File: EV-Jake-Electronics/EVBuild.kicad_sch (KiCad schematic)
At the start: 15 parts, among them J1 Spark Max PWM Pins, J2 Spark Max PWM Pins, U1 ESP32-S3-WROOM-2

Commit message: laser
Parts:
- removed C1: .1, symbol Device:C
- removed FlyDragon1: ~, symbol FlyDragon:FlyDragon
- removed J1: Spark Max PWM Pins, Connector_JST:JST_PH_S4B-PH-K_1x04_P2.00mm_Horizontal, symbol Connector:Conn_01x04_Socket
- removed LSF1: ~, symbol LSF0102:LSF0102
- removed R1: 220, symbol Device:R
- removed U1: ESP32-S3-WROOM-2, RF_Module:ESP32-S3-WROOM-2, symbol RF_Module:ESP32-S3-WROOM-2
- removed U2: ~, symbol LSF0104:LSF0104
- added C5: .1u, symbol Device:C
- added LSF2: ~, symbol LSF0104:LSF0104
- added R2: 220, symbol Device:R
- added R6, R7, R8, R9: 1k, Resistor_SMD:R_0201_0603Metric, symbol Device:R
- added SW1, SW2, SW3, SW4: SW_Push, Button_Switch_Keyboard:SW_Cherry_MX_1.00u_PCB, symbol Switch:SW_Push
- added U1: ESP32-WROOM-32, RF_Module:ESP32-WROOM-32, symbol RF_Module:ESP32-WROOM-32
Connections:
- net +5V: now also LSF2.7 (Vref_B), R2.1
- net 3V3: now also NCP1. (Vo), U1.2 (VDD)
- net CS: now also U1.24 (IO2)
- net FD 5V PWM: now also LSF2.7 (Vref_B)
- net GND: now also NCP1. (Vo), U3.1 (GND), C5.2, LSF2.6 (GND), R6.1, R7.1, R8.1, R9.1, U1.1 (GND), U1.15 (GND), U1.38 (GND), U1.39 (GND)
- net INT1: now also U1.14 (IO12)
- net INT2: now also U1.16 (IO13)
- net MISO: now also U1.29 (IO5)
- net MOSI: now also U1.26 (IO4)
- net SCK: now also U1.34 (RXD0/IO3)
- net SM 5V PWM 1: now also LSF2.8 (B2)
- net SM 5V PWM 2: now also LSF2.9 (B3)
- net VCC: now also NCP1. (Vo), U3.2 (VCC), R6.2, SW1.1, SW2.1, SW3.1, SW4.1, SW4.2, U1.12 (IO27)
- net OLED_SDA: now reaches U3.3 (SDA)
- net OLED_SDA: now also U1.33 (IO21)
- net OLED_SCL: now reaches U3.4 (SCL)
- net OLED_SCL: now also U1.36 (IO22)
- new net: C5.1, R2.2
- new net +3V3: LSF2.1 (Vref_A)
- new net BTN0: R9.2, SW1.2, U1.37 (IO23)
- new net BTN1: R8.2, SW2.2, U1.10 (IO25)
- new net BTN2: R7.2, SW3.2, U1.11 (IO26)
- new net FD 3V3 PWM: LSF2.2 (A1), U1.27 (IO16)
- new net SM 3V3 PWM 1: LSF2.3 (A2), U1.23 (IO15)
- new net SM 3V3 PWM 2: LSF2.4 (A3), U1.13 (IO14)
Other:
- note added: "Accelerometer"
- note added: "Battery"
- note added: "User Interface"
- moved on the sheet: FlyDragon2, NCP1

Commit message: .
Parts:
- added Laser1: ~, symbol laser:Laser
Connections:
- no-connect marks 4 -> 6
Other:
- note added: "Laser"
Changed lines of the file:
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@@
   (no_connect (at 254 114.3))
   (no_connect (at 254 119.38))
+  (no_connect (at 207.01 36.83))
+  (no_connect (at 226.06 36.83))
   (wire (pts (xy 209.55 115.57) (xy 209.55 104.14))
     (stroke (width 0) (type default))
@@
     (stroke (width 0) (type default))
   )
+  (rectangle (start 35.56 91.44) (end 54.61 119.38)
+    (stroke (width 0) (type default))
+    (fill (type none))
+  )
   (rectangle (start 186.69 13.97) (end 283.21 66.04)
     (stroke (width 0) (type default))
@@
   )
   (text "Battery" (at 15.24 74.93 0)
+    (effects (font (size 1.27 1.27)) (justify left bottom))
+  )
+  (text "Laser\n" (at 36.83 116.84 0)
     (effects (font (size 1.27 1.27)) (justify left bottom))
   )
@@
     )
   )
+  (symbol (lib_id "laser:Laser") (at 44.45 109.22 0) (unit 1)
+    (in_bom yes) (on_board yes) (dnp no) (fields_autoplaced)
+    (property "Reference" "Laser1" (at 46.99 102.87 0)
+      (effects (font (size 1.27 1.27)) (justify left))
+    )
+    (property "Value" "~" (at 34.29 113.03 0)
+      (effects (font (size 1.27 1.27)))
+    )
+    (property "Footprint" "" (at 34.29 113.03 0)
+      (effects (font (size 1.27 1.27)) hide)
+    )
+    (property "Datasheet" "" (at 34.29 113.03 0)
+      (effects (font (size 1.27 1.27)) hide)
+    )
+    (pin "")
+    (pin "")
+    (instances
+      (project "EVBuild"
+        (path "/2997cb29-a416-41db-a9e8-1a576f951325"
+          (reference "Laser1") (unit 1)
+        )
+      )
+    )
+  )
   (symbol (lib_id "Switch:SW_Push") (at 45.72 163.83 0) (unit 1)
     (in_bom yes) (on_board yes) (dnp no)
@@
         )
       )
+    )
+  )
+  (symbol (lib_id "power:GND") (at 245.11 214.63 0) (unit 1)
+    (in_bom yes) (on_board yes) (dnp no) (fields_autoplaced)
+    (property "Reference" "#PWR06" (at 245.11 220.98 0)
+      (effects (font (size 1.27 1.27)) hide)
+    )
+    (property "Value" "GND" (at 245.11 219.71 0)
+      (effects (font (size 1.27 1.27)))
+    )
+    (property "Footprint" "" (at 245.11 214.63 0)
+      (effects (font (size 1.27 1.27)) hide)
+    )
+    (property "Datasheet" "" (at 245.11 214.63 0)
+      (effects (font (size 1.27 1.27)) hide)
+    )
+    (pin "1")
+    (instances
+      (project "EVBuild"
+        (path "/2997cb29-a416-41db-a9e8-1a576f951325"
+          (reference "#PWR06") (unit 1)
+        )
+      )

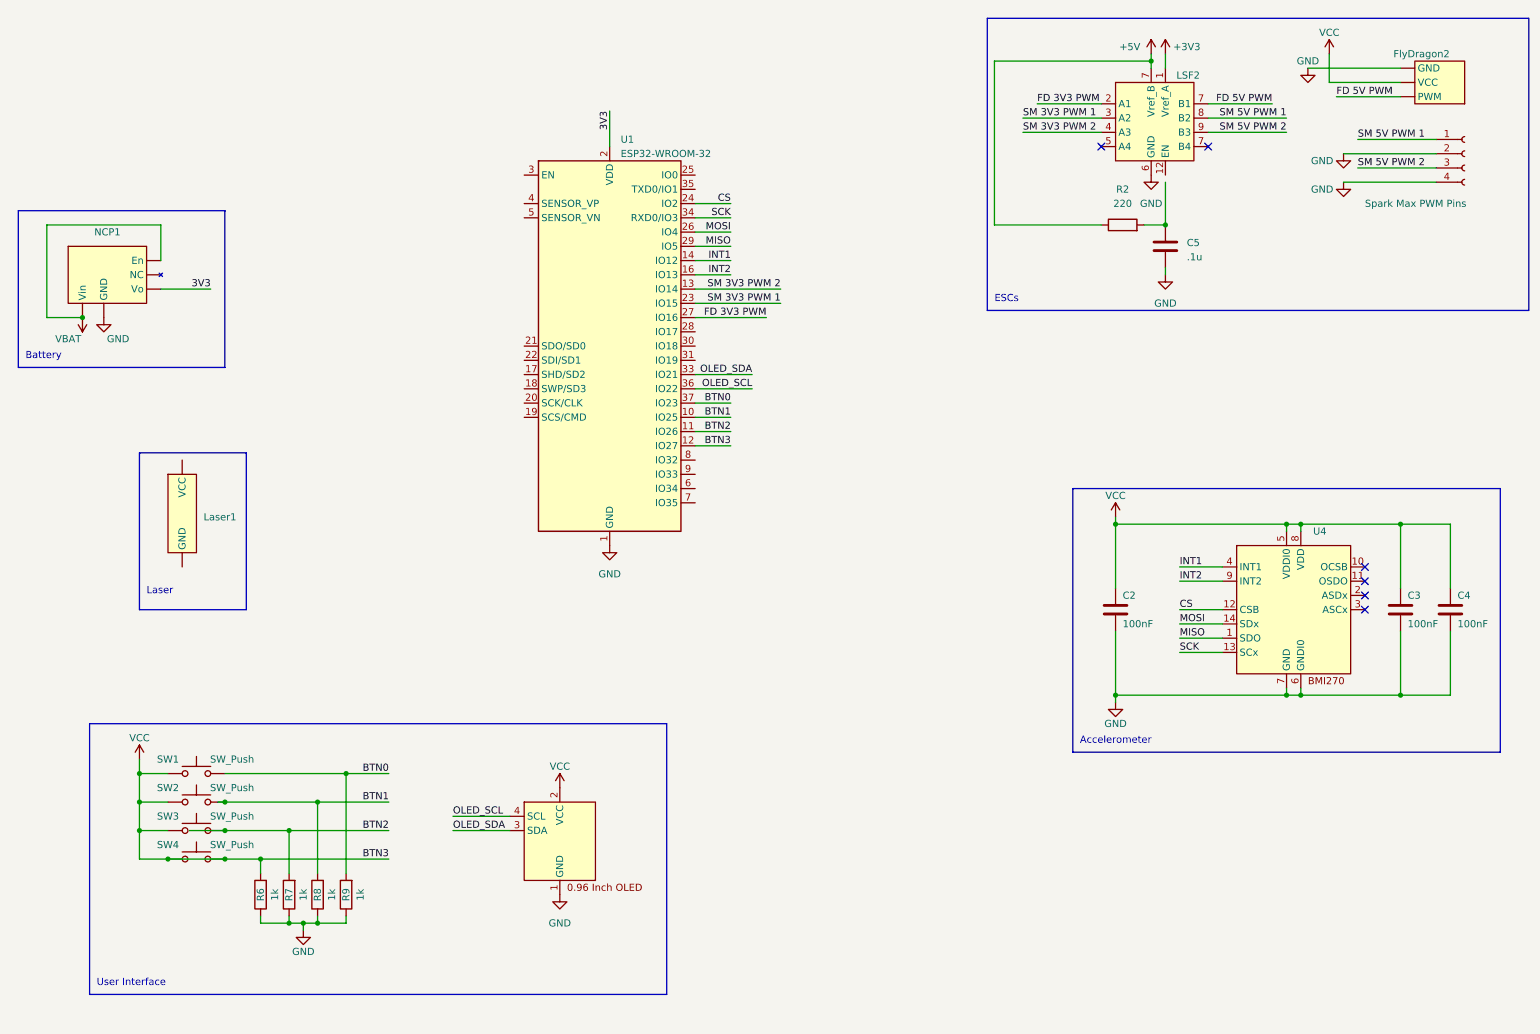
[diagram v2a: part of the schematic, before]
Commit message: fixed voltage regulator, switched out board, added encoder
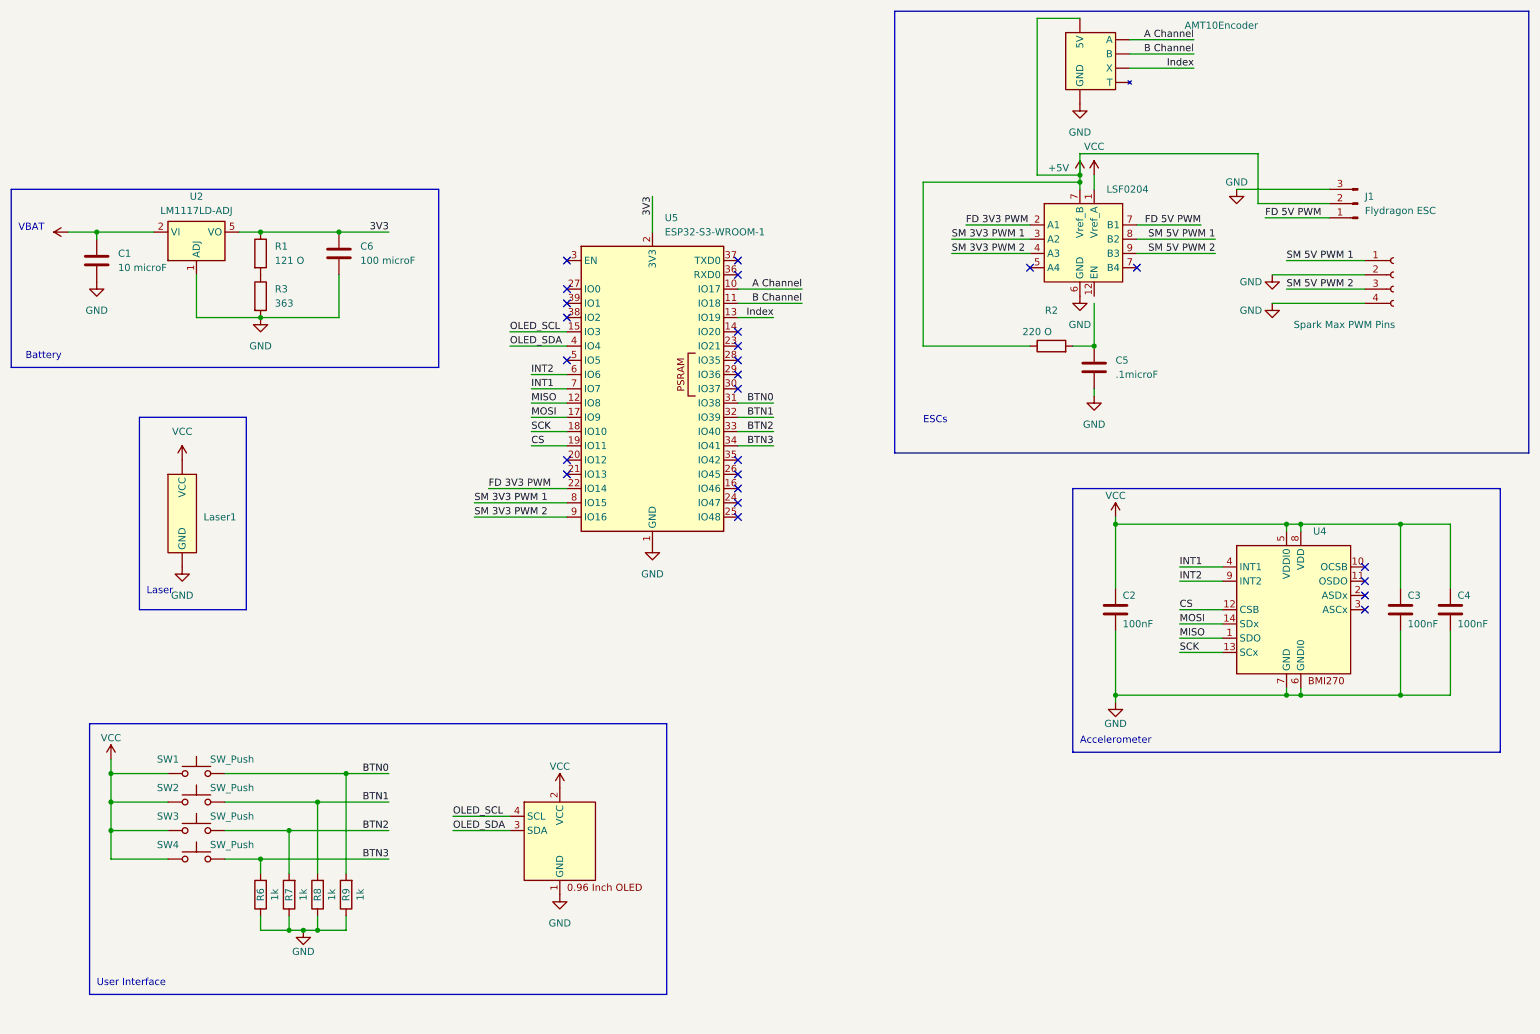
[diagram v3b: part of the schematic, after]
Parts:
- removed FlyDragon2: ~, symbol FlyDragon:FlyDragon
- removed NCP1: ~, symbol NCP551:NCP551
- removed U1: ESP32-WROOM-32, RF_Module:ESP32-WROOM-32, symbol RF_Module:ESP32-WROOM-32
- added AMT10Encoder: ~, symbol AMT10Enc:AMT10_Encoder
- added C1: 10 microF, symbol Device:C
- added C6: 100 microF, symbol Device:C
- added J1: Flydragon ESC, symbol Connector:Conn_01x03_Pin
- added R1: 121 O, symbol Device:R
- added R3: 363, symbol Device:R
- added U2: LM1117LD-ADJ, Package_SON:WSON-8-1EP_4x4mm_P0.8mm_EP2.2x3mm, symbol Regulator_Linear:LM1117LD-ADJ
- added U5: ESP32-S3-WROOM-1, RF_Module:ESP32-S3-WROOM-1, symbol RF_Module:ESP32-S3-WROOM-1
- C5: value .1u -> .1microF
- R2: value 220 -> 220 O
- renumbered LSF2 to LSF0204
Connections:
- net +3V3 is gone; now on net VCC: LSF0204.1 (Vref_A)
- net +5V: now also AMT10Encoder. (X), J1.2 (Pin_2)
- net 3V3: now also C6.1, R1.1, U2.5 (VO), U2.6 (VO), U2.7 (VO), U2.9 (VO), U5.2 (3V3)
- net BTN0: now also U5.31 (IO38)
- net BTN1: now also U5.32 (IO39)
- net BTN2: now also U5.33 (IO40)
- net CS: now also U5.19 (IO11)
- net FD 3V3 PWM: now also U5.22 (IO14)
- net FD 5V PWM: now also J1.1 (Pin_1)
- net GND: now also Laser1. (VCC), AMT10Encoder. (X), C1.2, C6.2, J1.3 (Pin_3), R3.2, U2.1 (ADJ), U5.1 (GND), U5.40 (GND), U5.41 (GND)
- net INT1: now also U5.7 (IO7)
- net INT2: now also U5.6 (IO6)
- net MISO: now also U5.12 (IO8)
- net MOSI: now also U5.17 (IO9)
- net OLED_SCL: now also U5.15 (IO3)
- net OLED_SDA: now also U5.4 (IO4)
- net SCK: now also U5.18 (IO10)
- net SM 3V3 PWM 1: now also U5.8 (IO15)
- net SM 3V3 PWM 2: now also U5.9 (IO16)
- net VCC: now also Laser1. (VCC), C1.1, U2.2 (VI), U2.3 (VI), U2.4 (VI); no longer R6.2, SW4.2
- new net: R1.2, R3.1
- new net A Channel: AMT10Encoder. (X), U5.10 (IO17)
- new net B Channel: AMT10Encoder. (X), U5.11 (IO18)
- new net BTN3: R6.2, SW4.2, U5.34 (IO41)
- new net Index: AMT10Encoder. (X), U5.13 (IO19)
- no-connect marks 6 -> 25
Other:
- note added: "VBAT"
- moved on the sheet: C5, LSF0204, R2

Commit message: switched from lm1117 to lm317 cuz we already have 317s
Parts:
- removed C6: 100 microF, symbol Device:C
- removed U2: LM1117LD-ADJ, Package_SON:WSON-8-1EP_4x4mm_P0.8mm_EP2.2x3mm, symbol Regulator_Linear:LM1117LD-ADJ
- added Co: .1microF, symbol Device:C
- added D1, D2: 1N4002, Diode_THT:D_DO-41_SOD81_P10.16mm_Horizontal, symbol Diode:1N4002
- added U1: LM317_TO3, Package_TO_SOT_THT:TO-3, symbol Regulator_Linear:LM317_TO3
- C1: value 10 microF -> .1microF
- R1: value 121 O -> 400 O
- R3: value 363 -> 240 O
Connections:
- net 3V3: now also R3.1, R3.2, Co.1, D1.2 (A), D2.1 (K), U1.1 (ADJ), U1.3 (VO)
- net GND: now also R1.2, Co.2, D2.2 (A); no longer R3.2
- net VCC: now also D1.1 (K), U1.2 (VI)
- net at C5.1, R2.2: now also LSF0204.12 (EN)

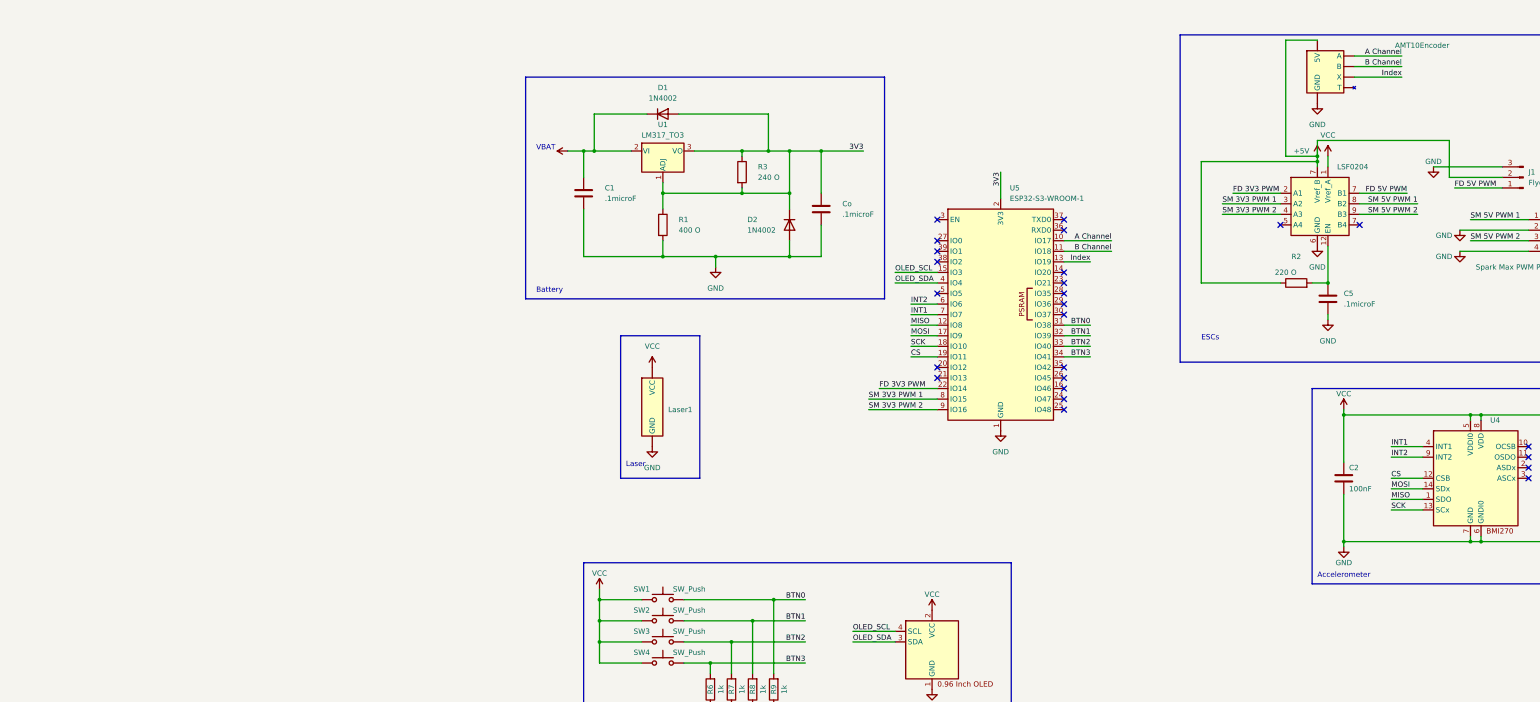
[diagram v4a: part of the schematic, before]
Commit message: usb to uart interface FSUSB74
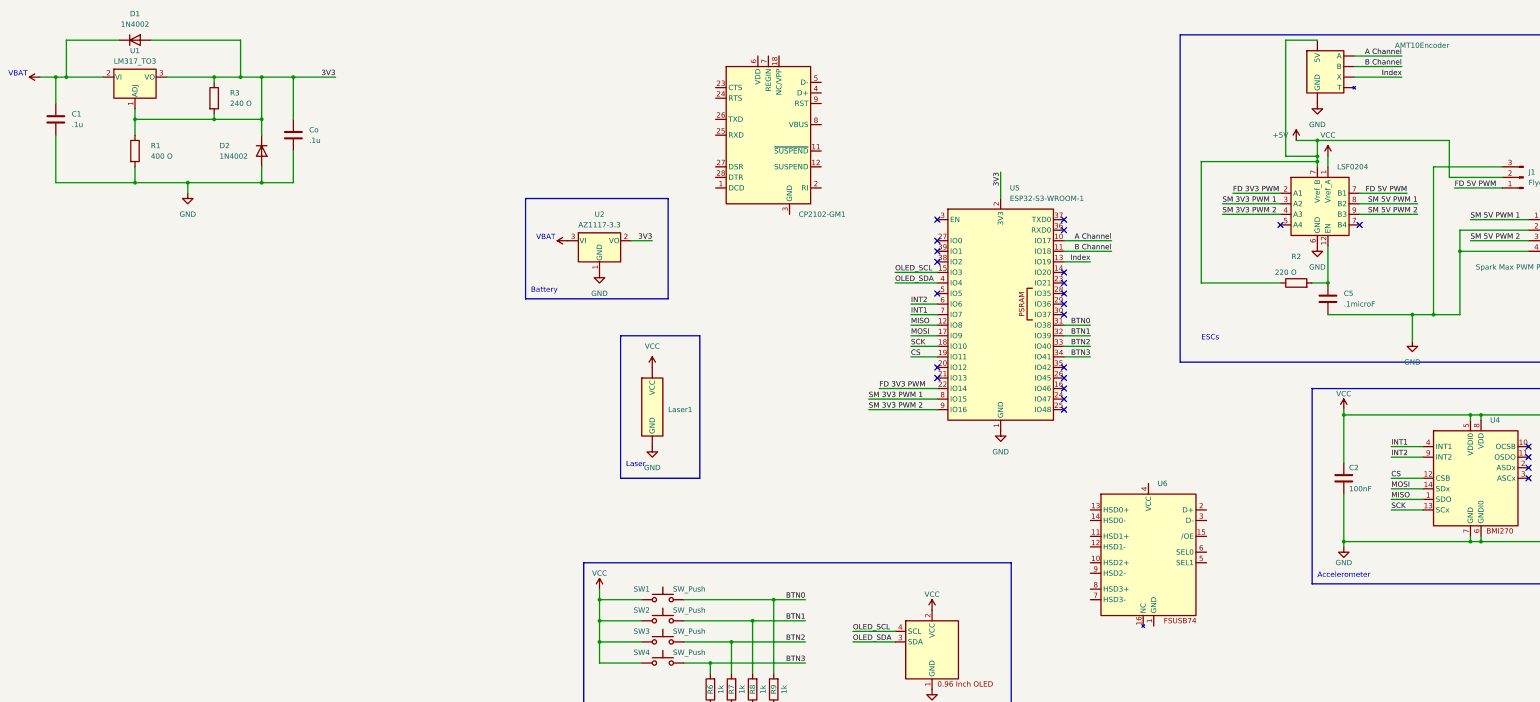
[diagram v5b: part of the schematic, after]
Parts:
- added CP2102-GM1: ~, Package_DFN_QFN:QFN-28-1EP_5x5mm_P0.5mm_EP3.1x3.1mm, symbol CP2102-GM:CP2102-GM
- added U2: AZ1117-3.3, symbol Regulator_Linear:AZ1117-3.3
- added U6: ~, Package_DFN_QFN:QFN-16-1EP_3x3mm_P0.5mm_EP1.7x1.7mm, symbol FUSB74:FSUSB74
- C1, Co: value .1microF -> .1u
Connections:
- net 3V3: now also U2.2 (VO)
- net GND: now also U2.1 (GND)
- net VCC: now also U2.3 (VI)
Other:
- moved on the sheet: C1, Co, D1, D2, R1, R3, U1

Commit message: footprints for everything
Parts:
- removed CP2102-GM1: ~, Package_DFN_QFN:QFN-28-1EP_5x5mm_P0.5mm_EP3.1x3.1mm, symbol CP2102-GM:CP2102-GM
- removed Co: .1u, symbol Device:C
- removed D1, D2: 1N4002, Diode_THT:D_DO-41_SOD81_P10.16mm_Horizontal, symbol Diode:1N4002
- removed R1: 400 O, symbol Device:R
- removed R3: 240 O, symbol Device:R
- removed U1: LM317_TO3, Package_TO_SOT_THT:TO-3, symbol Regulator_Linear:LM317_TO3
- removed U6: ~, Package_DFN_QFN:QFN-16-1EP_3x3mm_P0.5mm_EP1.7x1.7mm, symbol FUSB74:FSUSB74
- added BZ1: Buzzer, Buzzer_Beeper:Buzzer_12x9.5RM7.6, symbol Device:Buzzer
- added C6: 22uF, Capacitor_SMD:CP_Elec_6.3x5.9, symbol Device:C_Polarized
- added C7, C8: 100nF, Capacitor_SMD:C_0201_0603Metric, symbol Device:C
- added C9: 22u, Capacitor_THT:CP_Radial_D8.0mm_P5.00mm, symbol Device:C
- added D3: D, Resistor_SMD:R_0201_0603Metric, symbol Device:D
- added D4: LED, LED_SMD:LED_0603_1608Metric, symbol Device:LED
- added P1: USB_C_Plug_USB2.0, Connector_USB:USB_C_Receptacle_Molex_105450-0101, symbol Connector:USB_C_Plug_USB2.0
- added Q1: BC547, Package_TO_SOT_THT:TO-92_Inline, symbol Transistor_BJT:BC547
- added R10, R11, R4, R5: 1k, Resistor_SMD:R_0201_0603Metric, symbol Device:R
- added SW5: RST, Button_Switch_SMD:SW_SPST_TL3342, symbol Switch:SW_Push
- added SW6: ~{USB_BOOT}, Button_Switch_SMD:SW_DPDT_CK_JS202011JCQN, symbol Switch:SW_SPST
- added U6: AMS1117-3.3, Package_TO_SOT_SMD:SOT-223-3_TabPin2, symbol Regulator_Linear:AMS1117-3.3
- C1: value .1u -> 10u; footprint (none) -> Capacitor_THT:CP_Radial_D8.0mm_P5.00mm
- C5: value .1microF -> .1u; footprint (none) -> Capacitor_THT:CP_Radial_D8.0mm_P5.00mm
- LSF204: renamed from LSF0204; footprint (none) -> Package_SO:TSSOP-14_4.4x5mm_P0.65mm
- R2: value 220 O -> 220; footprint (none) -> Resistor_SMD:R_0201_0603Metric
- U2: footprint (none) -> Package_TO_SOT_SMD:SOT-223-3_TabPin2
- renumbered AMT10Encoder to AMT10Encoder1
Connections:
- net 3V3 is gone; now on net VCC: U2.2 (VO), U5.2 (3V3)
- net A Channel: now also U5.39 (IO1); no longer U5.10 (IO17)
- net B Channel: now also U5.38 (IO2); no longer U5.11 (IO18)
- net FD 3V3 PWM: now also U5.21 (IO13); no longer U5.22 (IO14)
- net GND: now also BZ1.2 (-), C6.2, C7.2, C8.2, C9.2, D4.2 (A), P1.A1 (GND), P1.A12 (GND), P1.B1 (GND), P1.B12 (GND), P1.S1 (SHIELD), R11.1, SW5.1, SW6.2 (B), U6.1 (GND)
- net Index: now also U5.15 (IO3); no longer U5.13 (IO19)
- net OLED_SCL: now also U5.4 (IO4); no longer U5.15 (IO3)
- net OLED_SDA: now also U5.5 (IO5); no longer U5.4 (IO4)
- net SM 3V3 PWM 1: now also U5.22 (IO14); no longer U5.8 (IO15)
- net SM 3V3 PWM 2: now also U5.8 (IO15); no longer U5.9 (IO16)
- net VCC: now also C6.1, C9.1, D3.2 (A), Q1.3 (E), R10.1, R4.1, U6.2 (VO); no longer Laser1. (VCC)
- net Buzzer: now reaches U5.14 (IO20)
- net Buzzer: now also BZ1.1 (+)
- net at U5.16 (IO46): now also R11.2
- net at U5.27 (IO0): now also C8.1, R4.2, SW6.1 (A)
- net at U5.3 (EN): now also C7.1, R10.2, SW5.2
- new net: D4.1 (K), R5.1
- new net: D3.1 (K), P1.A4 (VBUS), P1.A9 (VBUS), P1.B4 (VBUS), P1.B9 (VBUS), U6.3 (VI)
- new net: Laser1. (VCC), Q1.1 (C)
- new net: R5.2, U5.9 (IO16)
- new net D+: P1.A6 (D+), U5.13 (IO19)
- new net D-: P1.A7 (D-), U5.11 (IO18)
- new net Laser: Q1.2 (B), U5.10 (IO17)
- no-connect marks 25 -> 19
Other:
- note added: "USB Interface"
- moved on the sheet: AMT10Encoder1, C2, C3, C4, C5, J1, LSF204, Laser1, R2, R6, R7, R8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
